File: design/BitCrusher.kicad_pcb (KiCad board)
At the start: 2 copper layers, 181.5 x 86.2 mm, 136 parts, among them J1 BNC, J10 PJ-002BH, J2 BWSMA-KWE-Z001, J3 BWSMA-KE-Z001, J4 BWSMA-KE-Z001, J5 SHOU HAN TYPE-C 14P CC-2.6, J6 Conn_01x04_Pin, J7 Conn_01x04_Pin, J8 Conn_01x03_Pin, J9 Conn_01x03_Pin, Q1 SW4N60, Q2 2SA1213, Q3 GAN080-650EBE, T1 DA2033-AL, U1 STM32F303RETx, U2 USBLC6-2SC6, U3 FT230XQ, U4 TPS7A2050PDQN, U5 TPS7A2033PDQN, U6 LMR33630ADDA, U7 LMR33630ADDA, U8 TLP152TPL_E, U9 MAX22702EASA+

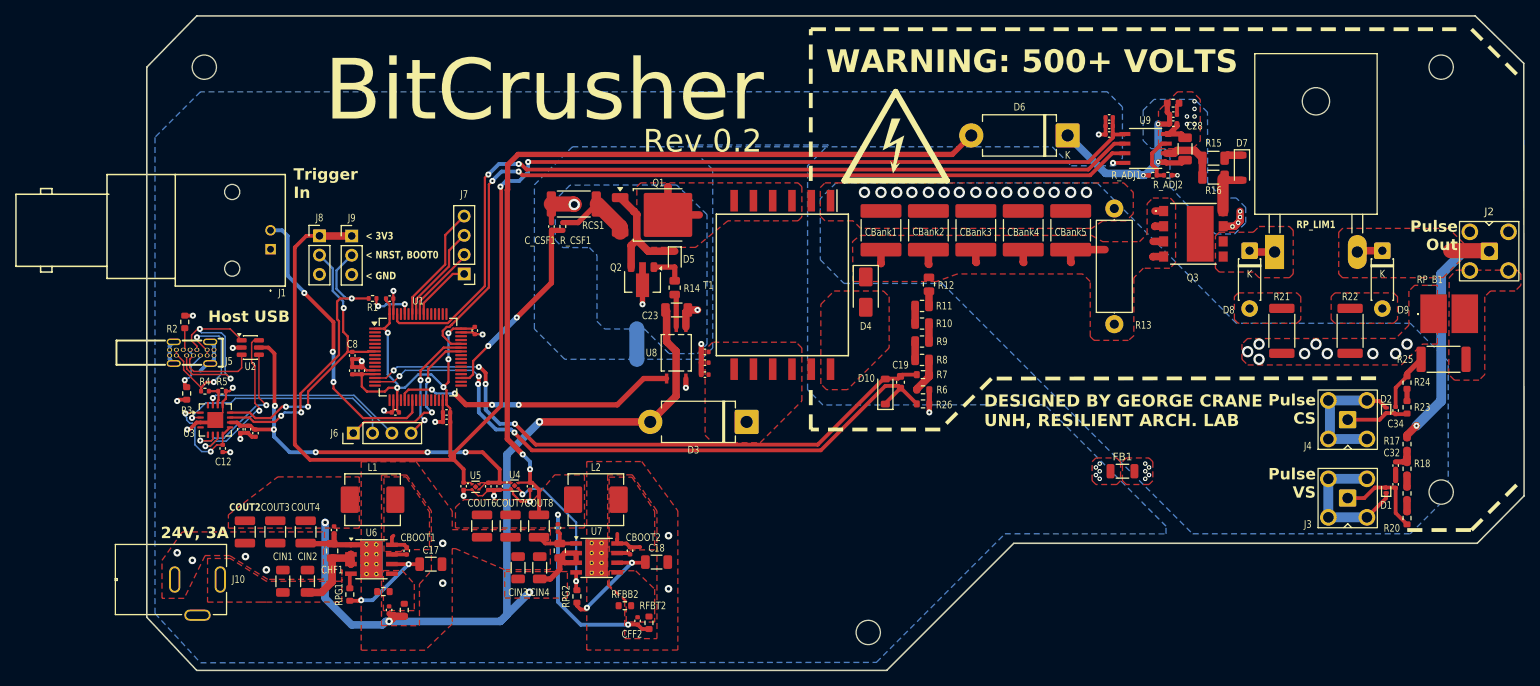
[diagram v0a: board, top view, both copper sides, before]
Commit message: Improved power supply filtering and surge protection
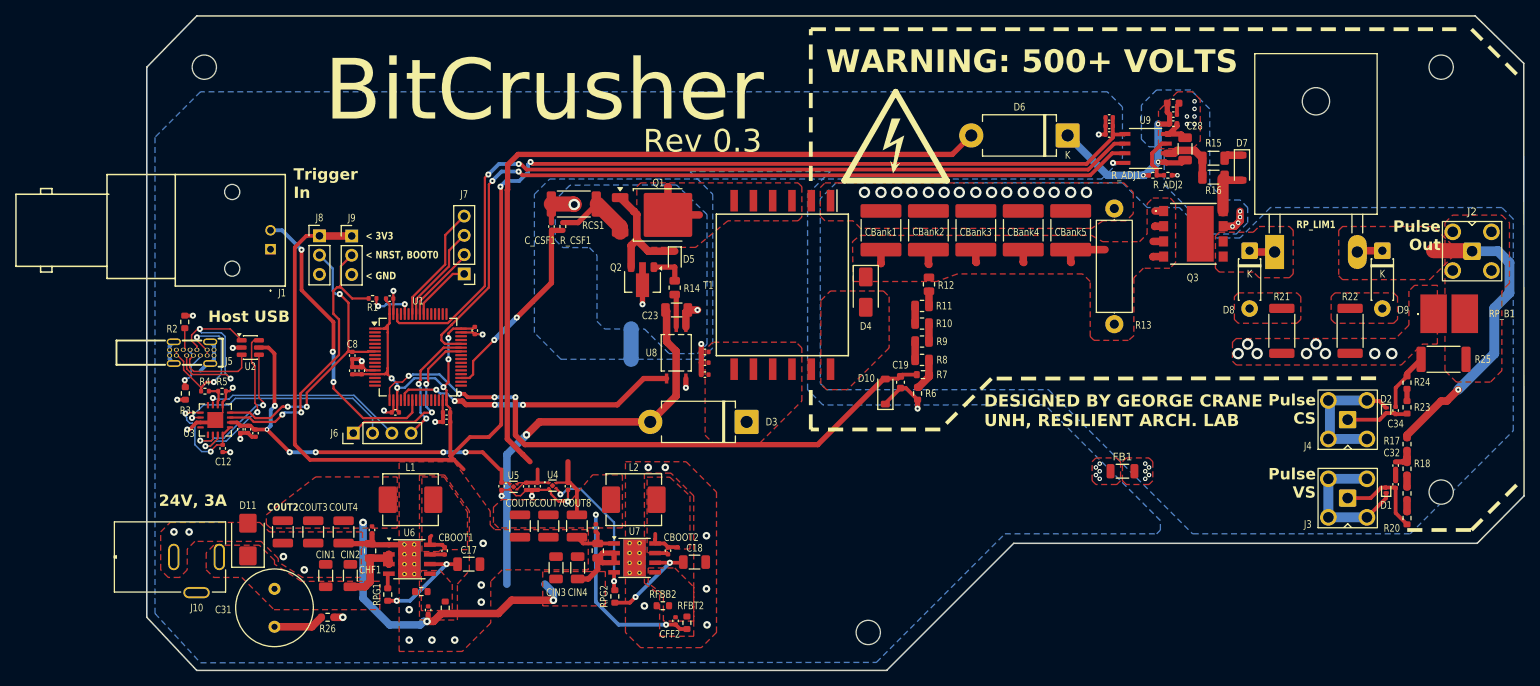
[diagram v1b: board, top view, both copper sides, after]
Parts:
- added C31: 150u, Capacitor_THT:C_Radial_D10.0mm_H20.0mm_P5.00mm, F.Cu at (75.8, 129.2)
- added D11: SMBJ20A, Diode_SMD:D_SMB, F.Cu at (72.2, 122.8)
- R26: value 0 -> 33m
- R6: value 60k -> 10k
- moved R26 83.4 mm to (82.8, 133.0), turned to 0 degrees
- moved CIN1 5.70 mm to (82.5, 127.5)
- moved CIN2 5.70 mm to (85.8, 127.5)
- moved RFBT1 5.41 mm to (98.2, 131.8)
- moved CFF1 5.15 mm to (96.0, 132.0)
- moved C13 5.00 mm to (114.4, 115.7)
- moved C14 5.00 mm to (110.4, 115.7)
- moved C15 5.00 mm to (108.9, 115.8)
- moved C16 5.00 mm to (105.7, 115.7)
- moved C17 5.00 mm to (101.4, 126.0)
- moved C18 5.00 mm to (131.1, 125.7)
- moved CBOOT1 5.00 mm to (98.2, 124.2)
- moved CBOOT2 5.00 mm to (127.6, 124.2)
- moved CFF2 5.00 mm to (128.6, 133.5)
- moved CHF1 5.00 mm to (88.4, 124.2)
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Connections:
- C19 pad 1: HVVS- -> GND
- D10 pad 1: HVVS- -> GND
- R26 pad 1: GND -> Net-(C31-Pad2)
- R26 pad 2: HVVS- -> GND
- U1 pad 14: HVVS+ -> unconnected-(U1-PA0-Pad14)
- U1 pad 15: HVVS- -> unconnected-(U1-PA1-Pad15)
- U1 pad 17: unconnected-(U1-PA3-Pad17) -> HVVS+
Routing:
- net HVVS-: track 86.8 -> 0.00 mm, vias 4 -> 0
- net +22V: track 114.1 -> 106.7 mm
- net Net-(C31-Pad2): track 0.00 -> 6.69 mm
- net GND: track 83.9 -> 88.8 mm, vias 32 -> 42
- net Probe+: track 40.5 -> 43.8 mm
- net +3V3: track 244.0 -> 241.5 mm
- net Net-(U7-VCC): track 14.2 -> 13.2 mm
- net +24V: track 11.9 -> 10.9 mm
- net HVVS+: track 83.1 -> 82.4 mm
- net Net-(U3-USBDP): track 20.1 -> 19.5 mm
- net +5V: track 58.7 -> 58.5 mm, vias 5 -> 6
- net BOOTSEL: track 39.4 -> 39.5 mm, vias 3 -> 2
- net +6V: vias 4 -> 2
- net PulseCS-: vias 29 -> 28
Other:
- board text added: "Rev 0.3"
- board text removed: "Rev 0.2"

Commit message: _
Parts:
- moved R25 0.50 mm to (229.8, 99.5)
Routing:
- net PulseCS-: vias 28 -> 29
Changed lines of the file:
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@@
 	(footprint "Resistor_SMD:R_2512_6332Metric"
 		(layer "F.Cu")
-		(at 229.815 99 180)
+		(at 229.815 99.5 180)
 		(descr "Resistor SMD 2512 (6332 Metric), square (rectangular) end terminal, IPC-7351 nominal, (Body size source: IPC-SM-782 page 72, https://www.pcb-3d.com/wordpress/wp-content/uploads/ipc-sm-782a_amendment_1_and_2.pdf), generated with kicad-footprint-generator")
 		(tags "resistor")
@@
 	)
 	(via
-		(at 223 98.25)
+		(at 223.25 98)
 		(size 1.5)
 		(drill 0.9)
@@
 	)
 	(via
+		(at 225 96.5)
+		(size 1.5)
+		(drill 0.9)
+		(layers "F.Cu" "B.Cu")
+		(free yes)
+		(capping no)
+		(covering
+			(front no)
+			(back no)
+		)
+		(plugging
+			(front no)
+			(back no)
+		)
+		(filling no)
+		(net "PulseCS-")
+	)
+	(via
 		(at 172.25 77)
 		(size 1.5)
@@
 	)
 	(segment
-		(start 73.7 104.076)
-		(end 73.7 98.4)
-		(width 0.2)
-		(layer "F.Cu")
-		(net "Net-(U3-USBDP)")
-	)
-	(segment
-		(start 74.25 105.051)
-		(end 74.25 104.626)
+		(start 74.25 103.25)
+		(end 73.7 102.7)
 		(width 0.2)
 		(layer "F.Cu")
@@
 	)
 	(segment
-		(start 74.25 104.626)
-		(end 73.7 104.076)
+		(start 74.25 105.051)
+		(end 74.25 103.25)
+		(width 0.2)
+		(layer "F.Cu")
+		(net "Net-(U3-USBDP)")
+	)
+	(segment
+		(start 73.7 102.7)
+		(end 73.7 98.4)
 		(width 0.2)
 		(layer "F.Cu")
@@
 	)
 	(segment
-		(start 66.643558 110.45)
-		(end 66.656922 110.463364)
-		(width 0.2)
-		(layer "F.Cu")
-		(net "Net-(U3-USBDM)")
-	)
-	(segment
-		(start 73.175 99.876)
-		(end 72.7365 99.4375)
-		(width 0.2)
-		(layer "F.Cu")
-		(net "Net-(U3-USBDM)")
-	)
-	(segment
-		(start 73.491785 105.964644)
-		(end 73.491785 105.123405)
+		(start 73.037501 96.5)
+		(end 73.7 96.5)
 		(width 0.2)
 		(layer "F.Cu")
@@
 	)
 	(segment
-		(start 72.7365 96.801001)
-		(end 73.037501 96.5)
+		(start 66.643558 110.45)
+		(end 66.656922 110.463364)
 		(width 0.2)
 		(layer "F.Cu")
@@
 	)
 	(segment
-		(start 72.7365 99.4375)
+		(start 72.7365 103.1115)
 		(end 72.7365 96.801001)
 		(width 0.2)
@@
 	)
 	(segment
-		(start 73.491785 105.123405)
-		(end 73.175 104.80662)
+		(start 73.491785 103.866785)
+		(end 72.7365 103.1115)
 		(width 0.2)
 		(layer "F.Cu")
@@
 	)
 	(segment
-		(start 73.037501 96.5)
-		(end 73.7 96.5)
+		(start 72.7365 96.801001)
+		(end 73.037501 96.5)
 		(width 0.2)
 		(layer "F.Cu")
@@
 	)
 	(segment
-		(start 73.175 104.80662)
-		(end 73.175 99.876)
+		(start 67.278736 110.463364)
+		(end 68.275 109.4671)
 		(width 0.2)
 		(layer "F.Cu")
@@
 	)
 	(segment
-		(start 67.278736 110.463364)
-		(end 68.275 109.4671)
+		(start 73.491785 105.964644)
+		(end 73.491785 103.866785)
 		(width 0.2)
 		(layer "F.Cu")
@@
 	)
 	(segment
-		(start 225 100.8525)
-		(end 226.8525 99)
+		(start 225.1025 101.25)
+		(end 226.79 99.5625)
 		(width 0.7)
 		(layer "F.Cu")
@@
 	)
 	(segment
-		(start 223.5 102.75)
-		(end 223.5 105.27)
-		(width 0.5)
+		(start 225 101.25)
+		(end 225.1025 101.25)
+		(width 0.7)
 		(layer "F.Cu")
 		(net "Net-(C34-Pad2)")
 	)
 	(segment
-		(start 225 101.25)
-		(end 225 100.8525)
+		(start 226.79 99.5625)
+		(end 226.79 99.0625)
 		(width 0.7)
 		(layer "F.Cu")
@@
 	)
 	(segment
-		(start 226.79 99.0625)
-		(end 226.8525 99)
-		(width 0.7)
+		(start 223.5 102.75)
+		(end 223.5 105.27)
+		(width 0.5)
 		(layer "F.Cu")
 		(net "Net-(C34-Pad2)")
@@
 	)
 	(segment
+		(start 80.675 134.25)
+		(end 81.925 133)
+		(width 1)
+		(layer "F.Cu")
+		(net "Net-(C31-Pad2)")
+	)
+	(segment
+		(start 75.75 134.25)
+		(end 80.675 134.25)
+		(width 1)
+		(layer "F.Cu")
+		(net "Net-(C31-Pad2)")
+	)
+	(segment
 		(start 221.75 84.69)
 		(end 218.62 84.69)
@@
 	)
 	(segment
-		(start 225 109)
-		(end 225 109.35)
-		(width 1)
-		(layer "F.Cu")
-		(net "Probe+")
-	)
-	(segment
-		(start 230.25 104.5)
-		(end 229.5 104.5)
+		(start 218.62 84.69)
+		(end 218.45 84.86)
 		(width 1)
 		(layer "F.Cu")
@@
 	)
 	(segment
-		(start 218.62 84.69)
-		(end 218.45 84.86)
+		(start 231.75 103)
+		(end 225.4 109.35)
 		(width 1)
 		(layer "F.Cu")
@@
 	)
 	(segment
-		(start 231.75 103)
-		(end 230.25 104.5)
+		(start 225.4 109.35)
+		(end 225 109.35)
 		(width 1)
 		(layer "F.Cu")
@@
 		(net "Probe+")
 	)
-	(segment
-		(start 229.5 104.5)
-		(end 225 109)
-		(width 1)
-		(layer "F.Cu")
-		(net "Probe+")
-	)
 	(via
 		(at 231.75 103)
@@
 	)
 	(segment
-		(start 238.5 90.25)
-		(end 238.5 86.25)
-		(width 1.3)
-		(layer "B.Cu")
-		(net "Probe+")
-	)
-	(segment
 		(start 238.5 86.25)
 		(end 237 84.75)
@@
 	)
 	(segment
-		(start 236.5 98.25)
-		(end 236.5 92.25)
-		(width 1.3)
-		(layer "B.Cu")
-		(net "Probe+")
-	)
-	(segment
-		(start 231.75 103)
-		(end 236.5 98.25)
+		(start 238.5 96.25)
+		(end 238.5 86.25)
 		(width 1.3)
 		(layer "B.Cu")
@@
 	)
 	(segment
-		(start 236.5 92.25)
-		(end 238.5 90.25)
+		(start 237 84.75)
+		(end 233.575 84.75)
 		(width 1.3)
 		(layer "B.Cu")
@@
 	)
 	(segment
-		(start 237 84.75)
-		(end 233.575 84.75)
+		(start 231.75 103)
+		(end 238.5 96.25)
 		(width 1.3)
 		(layer "B.Cu")
@@
 	)
 	(segment
-		(start 123.102086 79.4935)
-		(end 121.301086 77.6925)
-		(width 1)
-		(layer "F.Cu")
-		(net "Net-(D5-K)")
-	)
-	(segment
 		(start 123.501086 83.252172)
 		(end 123.501086 79.9)
@@
 	)
 	(segment
-		(start 123.501086 79.9)
-		(end 123.102086 79.501)
+		(start 121.301086 77.7)
+		(end 121.301086 77.6925)
 		(width 1)
 		(layer "F.Cu")
@@
 	)
 	(segment
-		(start 123.102086 79.501)
-		(end 123.102086 79.4935)
+		(start 123.501086 79.9)
+		(end 121.301086 77.7)
 		(width 1)
 		(layer "F.Cu")
@@
 		(net "Net-(D7-A)")
 	)
-	(segment
-		(start 80.675 134.25)
-		(end 81.925 133)
-		(width 1)
-		(layer "F.Cu")
-		(net "Net-(C31-Pad2)")
-	)
-	(segment
-		(start 75.75 134.25)
-		(end 80.675 134.25)
-		(width 1)
-		(layer "F.Cu")
-		(net "Net-(C31-Pad2)")
-	)
 	(zone
 		(net "PulseCS-")
@@
 		(polygon
 			(pts
-				(xy 229 89.25) (xy 226 89.25) (xy 225.25 90) (xy 225.25 94.5) (xy 223.5 96.25) (xy 202.482645 96.267048)
+				(xy 229 89.25) (xy 226 89.25) (xy 225.25 90) (xy 225.25 93.75) (xy 222.749391 96.250609) (xy 202.482645 96.267048)
 				(xy 202 96.750333) (xy 202 99.25) (xy 202.5 99.75) (xy 224.25 99.75) (xy 227 97) (xy 229 97)
 			)
@@
 			(pts
 				(xy 124.499782 95) (xy 127.75 98.25) (xy 131.5 98.25) (xy 132.75 97) (xy 132.75 79.92197) (xy 128.7475 76.026821)
-				(xy 114.690627 76.050356) (xy 112.7475 78) (xy 112.7475 83.276821) (xy 113.7475 84.276821) (xy 117.2475 84.276821)
+				(xy 114.5 76.051183) (xy 112.75 77.75) (xy 112.75 82.5) (xy 114.5 84.25) (xy 117.2475 84.276821)
 				(xy 118.2475 85.276821) (xy 118.25 94) (xy 119.25 95)
 			)
@@
 			(pts
 				(xy 147.675 102.175) (xy 148.5 103) (xy 177.75 103) (xy 196.75 122) (xy 225.425 122) (xy 239 108.425)
-				(xy 239 80.5) (xy 237.50023 79) (xy 207 79) (xy 203 83) (xy 199 83) (xy 195 79) (xy 190.750016 79)
-				(xy 187.5 75.75) (xy 149.75 75.75) (xy 147.675 77.825)
+				(xy 239 80.5) (xy 236.500383 78) (xy 208 78) (xy 203 83) (xy 199 83) (xy 191.742652 75.75) (xy 149.75 75.75)
+				(xy 147.675 77.825)
 			)
 		)

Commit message: layout optimization
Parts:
- moved H1 87.5 mm to (66.5, 132.5)
- moved FB1 12.3 mm to (197.2, 106.2), turned to 45 degrees
- moved R26 6.17 mm to (77.5, 136.2)
- moved H2 3.50 mm to (233.0, 60.5)
- moved H3 3.50 mm to (233.0, 116.5)
- moved J10 3.08 mm to (69.8, 122.2)
- moved D11 2.69 mm to (73.2, 120.2)
- moved C31 2.02 mm to (76.8, 127.5)
- moved CIN1 1.00 mm to (83.5, 127.5)
- moved COUT2 0.90 mm to (77.8, 121.8)
- moved RP_B1 0.44 mm to (231.0, 93.0)
- moved COUT3 0.40 mm to (81.2, 121.8)
- moved CIN2 0.25 mm to (86.0, 127.5)
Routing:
- net PulseCS-: track 37.9 -> 46.4 mm, vias 29 -> 33
- net +22V: track 106.7 -> 111.8 mm, vias 4 -> 5
- net +5V: track 58.5 -> 63.6 mm
- net +6V: track 137.3 -> 142.3 mm
- net +3V3: track 241.5 -> 245.5 mm
- net Net-(C31-Pad2): track 6.69 -> 3.78 mm
- net +24V: track 10.9 -> 8.73 mm
- net GND: vias 42 -> 46

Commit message: Layout opt
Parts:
- moved NT1 15.6 mm to (111.2, 86.5), turned to 0 degrees
- moved L1 1.50 mm to (93.7, 119.0)
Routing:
- net HVCS: track 26.5 -> 30.9 mm
- net GNDFLY: track 18.0 -> 21.8 mm, vias 4 -> 5
- net +5V: track 63.6 -> 67.2 mm, vias 6 -> 4
- net GND: track 88.8 -> 92.4 mm, vias 46 -> 45
- net +22V: track 111.8 -> 114.2 mm, vias 5 -> 6
- net RX_IN: track 26.9 -> 28.4 mm, vias 1 -> 5
- net TX_IN: track 29.2 -> 30.6 mm, vias 1 -> 5
- net Net-(J5-D--PadA7): track 27.6 -> 26.6 mm
- net +3V3: track 245.5 -> 244.6 mm
- net Net-(U3-USBDM): track 21.8 -> 21.1 mm
- net Net-(U3-USBDP): track 19.5 -> 18.9 mm
- net PulseCS-: vias 33 -> 32

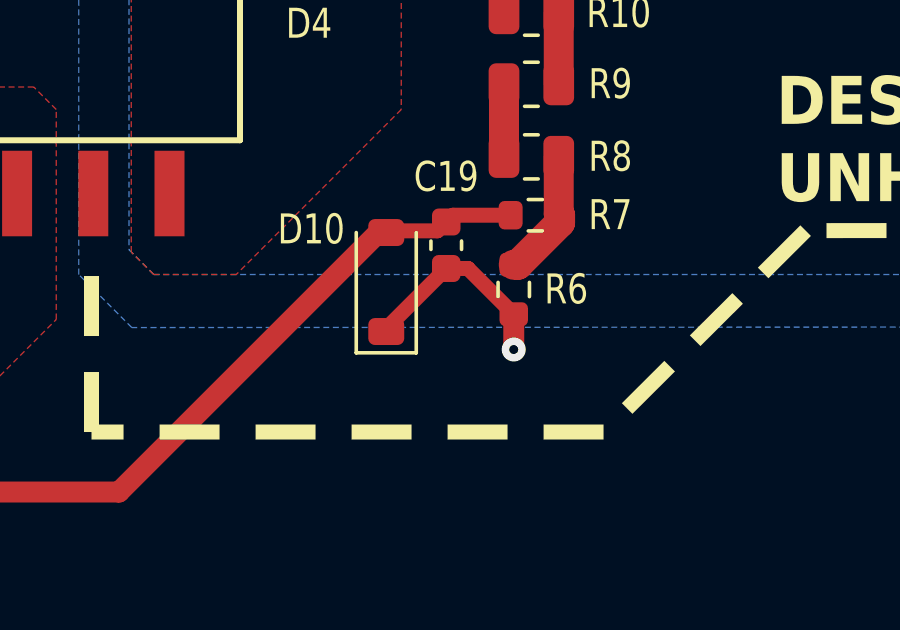
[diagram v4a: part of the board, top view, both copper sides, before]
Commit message: Changed TVS diodes on measurement bufferes to match 0-25V expected range.
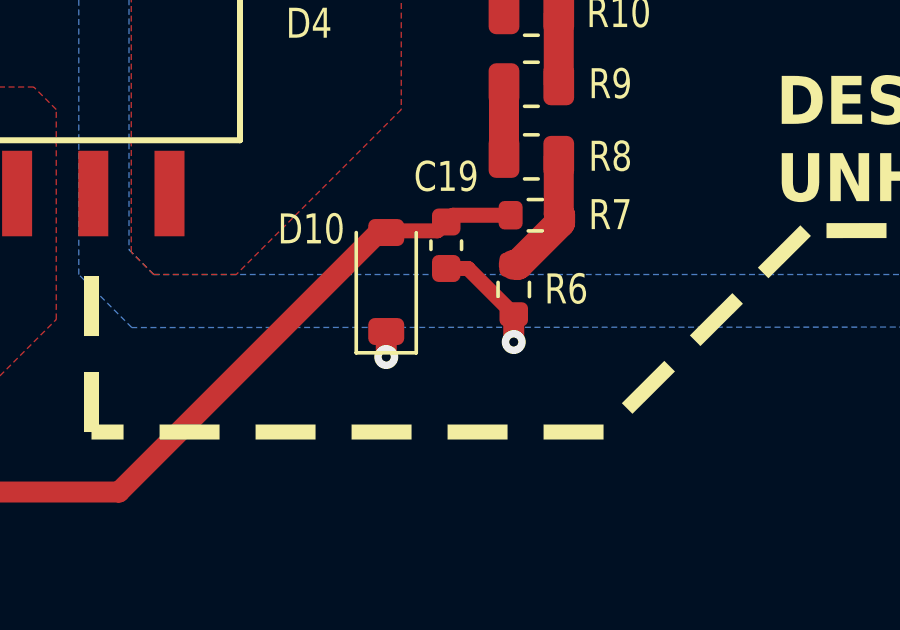
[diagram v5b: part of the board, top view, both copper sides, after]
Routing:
- net GND: track 92.4 -> 90.2 mm, vias 45 -> 46
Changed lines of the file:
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@@
+	)
+	(segment
+		(start 156.25 104.9)
+		(end 156.25 105.75)
+		(width 0.7)
+		(layer "F.Cu")
+		(net "GND")
 	)
 	(segment
@@
 	)
 	(segment
+		(start 160.5 105.25)
+		(end 160.5 104.325)
+		(width 0.7)
+		(layer "F.Cu")
+		(net "GND")
+	)
+	(segment
 		(start 112.183245 116.758245)
 		(end 112.183245 116.353701)
@@
 	)
 	(segment
-		(start 156.25 104.79875)
-		(end 158.25 102.79875)
-		(width 0.5)
-		(layer "F.Cu")
-		(net "GND")
-	)
-	(segment
 		(start 92.83 123.445)
 		(end 92.875 123.4)
@@
 		(net "GND")
 	)
-	(segment
-		(start 160.5 105.5)
-		(end 160.5 104.325)
-		(width 0.7)
-		(layer "F.Cu")
-		(net "GND")
-	)
 	(via
 		(at 194.5 108)
@@
 	)
 	(via
+		(at 156.25 105.75)
+		(size 0.8)
+		(drill 0.3)
+		(layers "F.Cu" "B.Cu")
+		(capping no)
+		(covering
+			(front no)
+			(back no)
+		)
+		(plugging
+			(front no)
+			(back no)
+		)
+		(filling no)
+		(net "GND")
+	)
+	(via
 		(at 98.25 135.5)
 		(size 1)
@@
 	)
 	(via
-		(at 160.5 105.5)
-		(size 0.8)
-		(drill 0.3)
+		(at 160.5 105.25)
+		(size 0.8)
+		(drill 0.3)
